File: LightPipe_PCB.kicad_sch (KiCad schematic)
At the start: 13 parts, among them J5 AudioJack4, X1 KLB-4, X2 KLB-4, X3 XT30, X4.1 Cable-0.7mm, X4.2 Cable-0.7mm, X5.1 Cable-1.5mm, X5.2 Cable-1.5mm

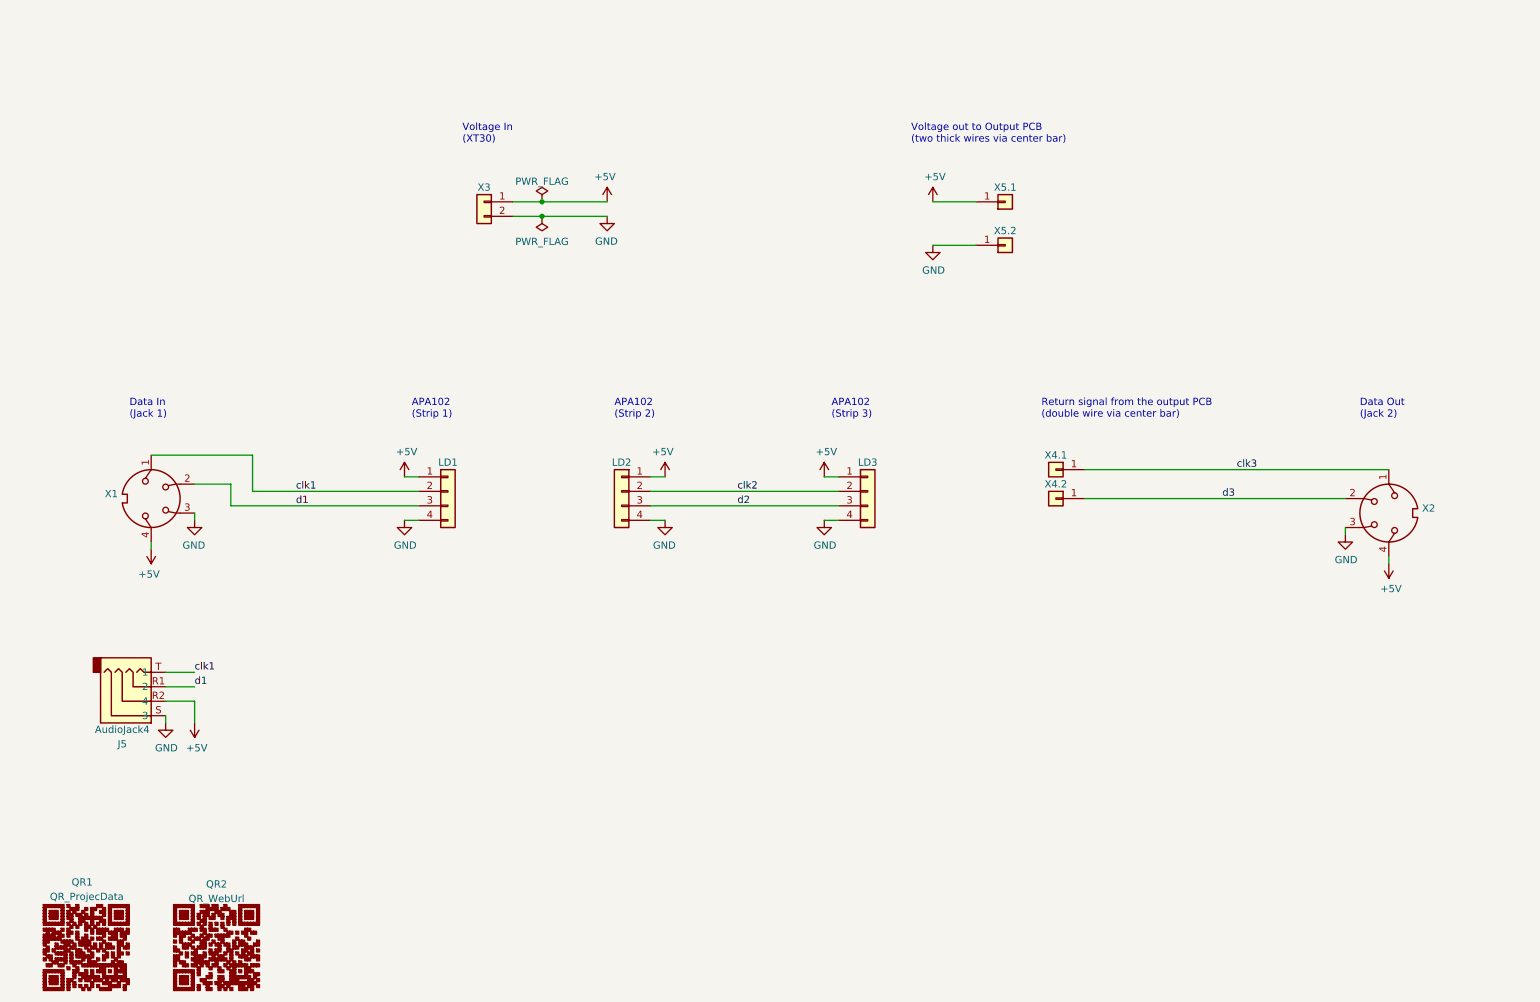
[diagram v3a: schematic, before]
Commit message: [clean] improved schematic and pcb to be easier to read in Input-Mode 2
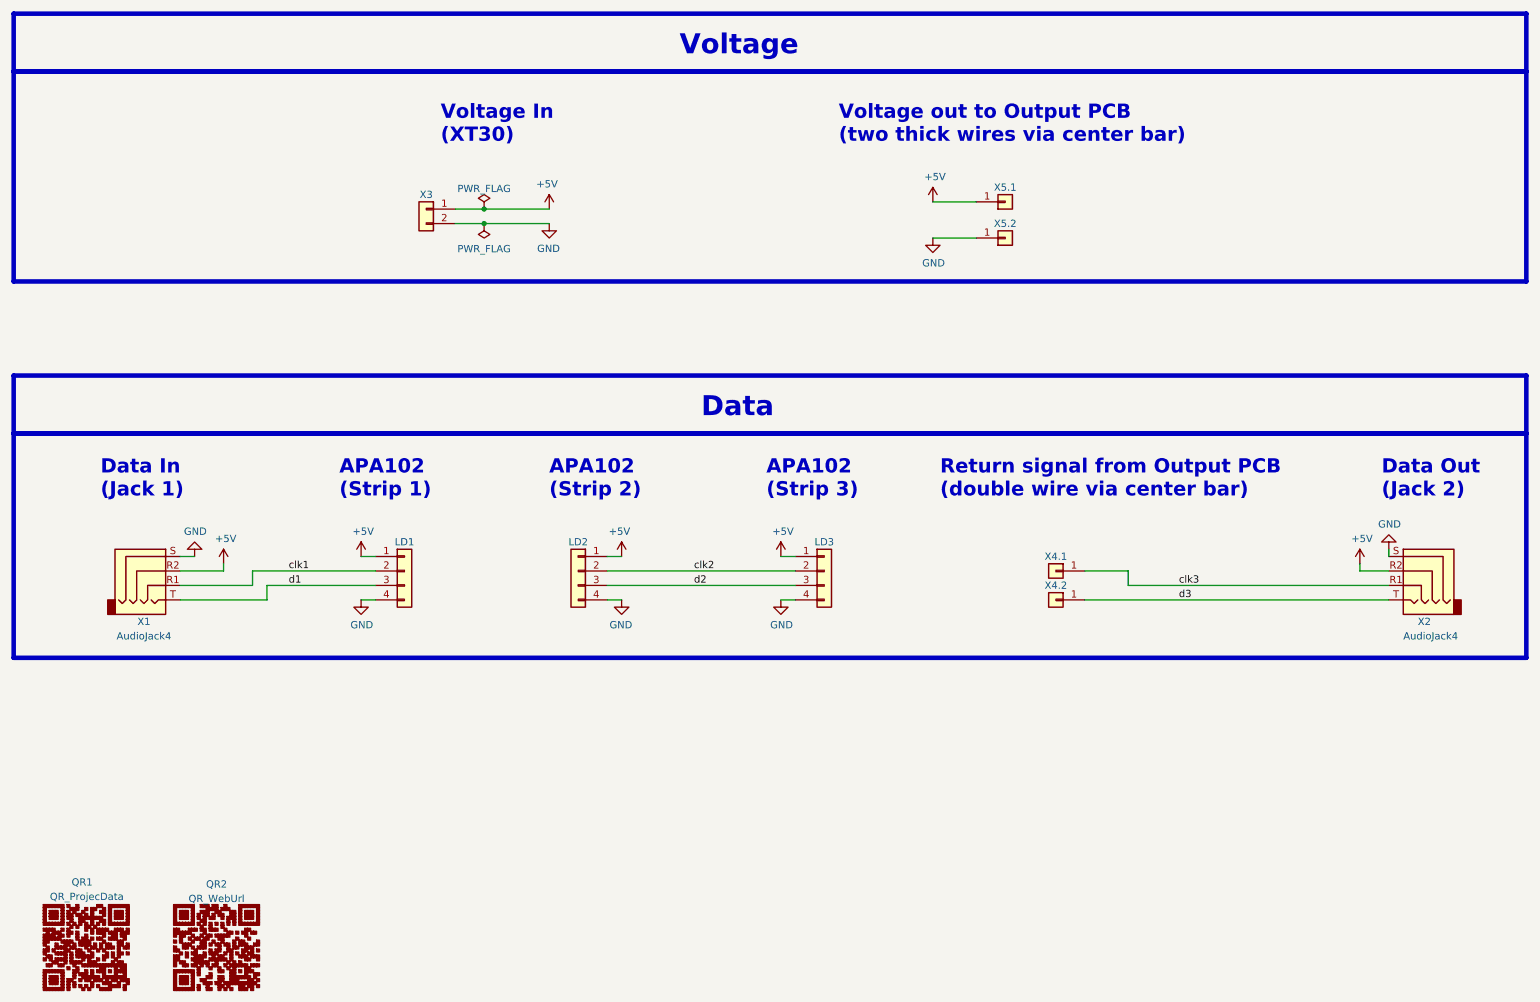
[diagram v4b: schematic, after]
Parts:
- removed X1, X2: KLB-4, h8-Connectors:Lumberg-KLB-4-Klinkensteckverbinder-3_5-180deg-turnable, symbol Connector:DIN-4
- added X2: AudioJack4, h8-Connectors:Lumberg-KLB-4-Jack-3_5-180deg-turnable, symbol Connector:AudioJack4
- QR1: footprint QR:QR_ProjecData -> QR_Lib:QR_ProjecData
- QR2: footprint QR:QR_WebUrl -> QR_Lib:QR_WebUrl
- X1: renamed from J5; footprint h8-Connectors:Lumberg-KLB-4-Klinkensteckverbinder-3_5-180deg-turnable -> h8-Connectors:Lumberg-KLB-4-Jack-3_5-180deg-turnable
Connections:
- net +5V: now also X2.R2
- net GND: now also X2.S
- net clk1: now also X1.R1; no longer X1.T
- net clk3: now also X2.R1
- net d1: now also X1.T; no longer X1.R1
- net d3: now also X2.T
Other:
- note added: "Data"
- note added: "Return signal from Output PCB (double wire via center bar)"
- note added: "Voltage"
- note removed: "Return signal from the output PCB (double wire via center bar)"
- moved on the sheet: LD1, LD2, LD3, X3, X4.1, X4.2, X5.2

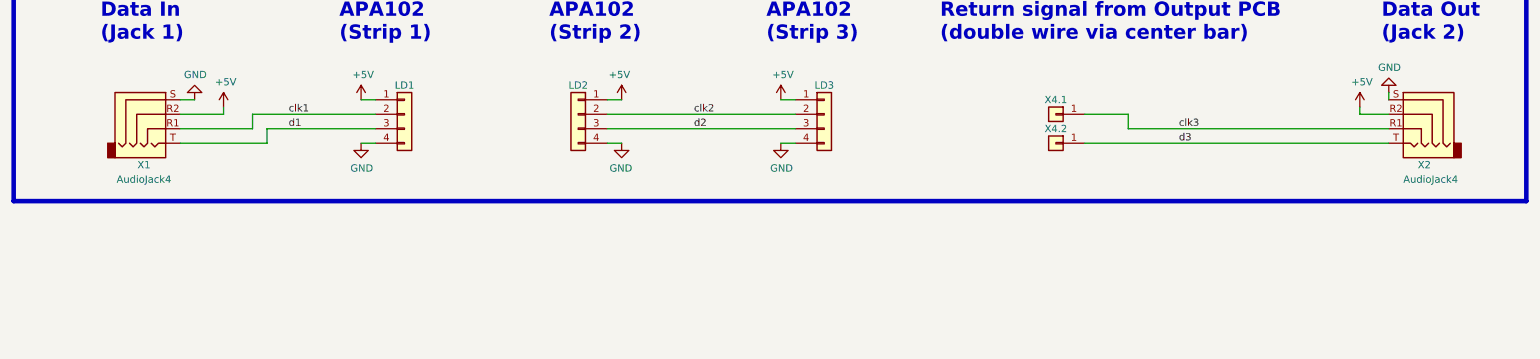
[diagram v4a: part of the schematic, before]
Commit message: [PCB] Fixed Fab layers | added attributes to components
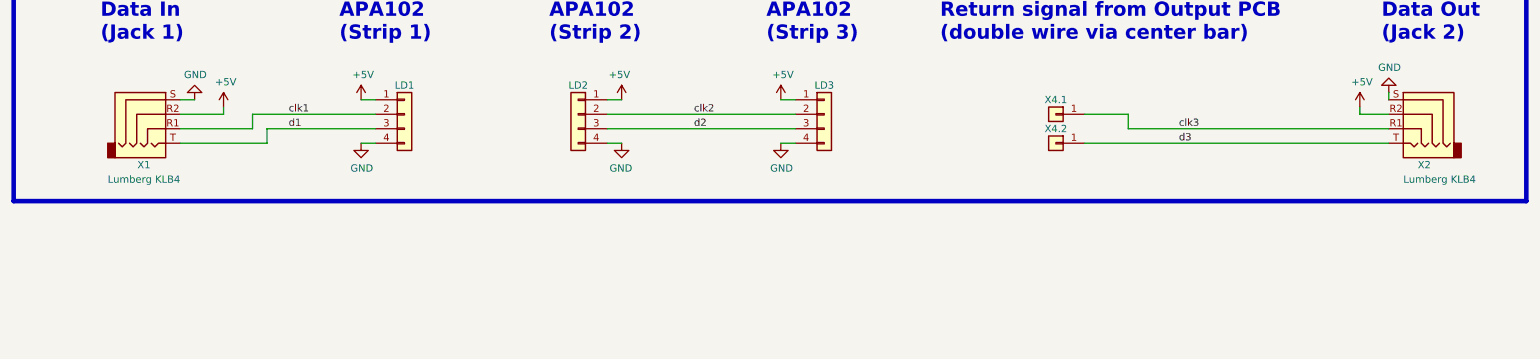
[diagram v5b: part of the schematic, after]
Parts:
- X1, X2: value AudioJack4 -> Lumberg KLB4; MF (none) -> Lumberg; MF1 (none) -> HUXUAN; MFN (none) -> KLB4; MFN1 (none) -> PJ392
- X3: LCSC (none) -> C108769; MF (none) -> Changzhou Amass Elec; MFN (none) -> XT30UPB30-F.G.*
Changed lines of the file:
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@@
       (effects (font (size 1.27 1.27)) hide)
     )
-    (property "Datasheet" "~" (id 3) (at 87.63 54.61 0)
+    (property "Datasheet" "https://datasheet.lcsc.com/lcsc/2207151430_Changzhou-Amass-Elec-XT30UPB30-F-G--_C108769.pdf" (id 3) (at 87.63 54.61 0)
+      (effects (font (size 1.27 1.27)) hide)
+    )
+    (property "MF" "Changzhou Amass Elec " (id 4) (at 87.63 54.61 0)
+      (effects (font (size 1.27 1.27)) hide)
+    )
+    (property "MFN" "XT30UPB30-F.G.*" (id 5) (at 87.63 54.61 0)
+      (effects (font (size 1.27 1.27)) hide)
+    )
+    (property "LCSC" "C108769" (id 6) (at 87.63 54.61 0)
       (effects (font (size 1.27 1.27)) hide)
     )
@@
     (in_bom yes) (on_board yes)
     (property "Reference" "X1" (id 0) (at 38.1 127 0))
-    (property "Value" "AudioJack4" (id 1) (at 38.1 129.54 0))
+    (property "Value" "Lumberg KLB4" (id 1) (at 38.1 129.54 0))
     (property "Footprint" "h8-Connectors:Lumberg-KLB-4-Jack-3_5-180deg-turnable" (id 2) (at 39.37 118.11 0)
       (effects (font (size 1.27 1.27)) hide)
     )
-    (property "Datasheet" "~" (id 3) (at 39.37 118.11 0)
+    (property "Datasheet" "https://downloads.lumberg.com/datenblaetter/en/klb4.pdf" (id 3) (at 39.37 118.11 0)
+      (effects (font (size 1.27 1.27)) hide)
+    )
+    (property "MF" "Lumberg" (id 4) (at 39.37 118.11 0)
+      (effects (font (size 1.27 1.27)) hide)
+    )
+    (property "MFN" "KLB4" (id 5) (at 39.37 118.11 0)
+      (effects (font (size 1.27 1.27)) hide)
+    )
+    (property "MF1" "HUXUAN" (id 6) (at 39.37 118.11 0)
+      (effects (font (size 1.27 1.27)) hide)
+    )
+    (property "MFN1" "PJ392" (id 7) (at 39.37 118.11 0)
       (effects (font (size 1.27 1.27)) hide)
     )
@@
       (effects (font (size 1.27 1.27)) (justify right))
     )
-    (property "Value" "AudioJack4" (id 1) (at 259.08 129.54 0)
+    (property "Value" "Lumberg KLB4" (id 1) (at 259.08 129.54 0)
       (effects (font (size 1.27 1.27)) (justify right))
     )
@@
       (effects (font (size 1.27 1.27)) hide)
     )
-    (property "Datasheet" "~" (id 3) (at 261.62 118.11 0)
+    (property "Datasheet" "https://downloads.lumberg.com/datenblaetter/en/klb4.pdf" (id 3) (at 261.62 118.11 0)
+      (effects (font (size 1.27 1.27)) hide)
+    )
+    (property "MF" "Lumberg" (id 4) (at 261.62 118.11 0)
+      (effects (font (size 1.27 1.27)) hide)
+    )
+    (property "MFN" "KLB4" (id 5) (at 261.62 118.11 0)
+      (effects (font (size 1.27 1.27)) hide)
+    )
+    (property "MF1" "HUXUAN" (id 6) (at 261.62 118.11 0)
+      (effects (font (size 1.27 1.27)) hide)
+    )
+    (property "MFN1" "PJ392" (id 7) (at 261.62 118.11 0)
       (effects (font (size 1.27 1.27)) hide)
     )
@@
     )
     (path "/67e54464-02b8-42b4-98cc-9748abe49e4c"
-      (reference "X1") (unit 1) (value "AudioJack4") (footprint "h8-Connectors:Lumberg-KLB-4-Jack-3_5-180deg-turnable")
+      (reference "X1") (unit 1) (value "Lumberg KLB4") (footprint "h8-Connectors:Lumberg-KLB-4-Jack-3_5-180deg-turnable")
     )
     (path "/7f404442-9c89-47ea-a816-5ae74e1d23ad"
-      (reference "X2") (unit 1) (value "AudioJack4") (footprint "h8-Connectors:Lumberg-KLB-4-Jack-3_5-180deg-turnable")
+      (reference "X2") (unit 1) (value "Lumberg KLB4") (footprint "h8-Connectors:Lumberg-KLB-4-Jack-3_5-180deg-turnable")
     )
     (path "/00000000-0000-0000-0000-00005f94666b"

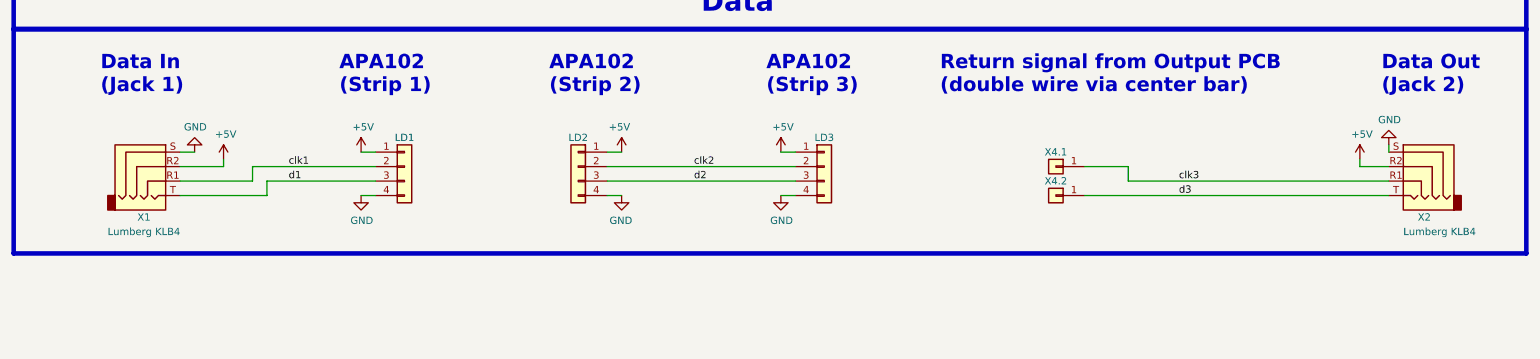
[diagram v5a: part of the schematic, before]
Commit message: [WIP] Optimize PCB for more common LED-Strip (GND, D, CLK, 5V)
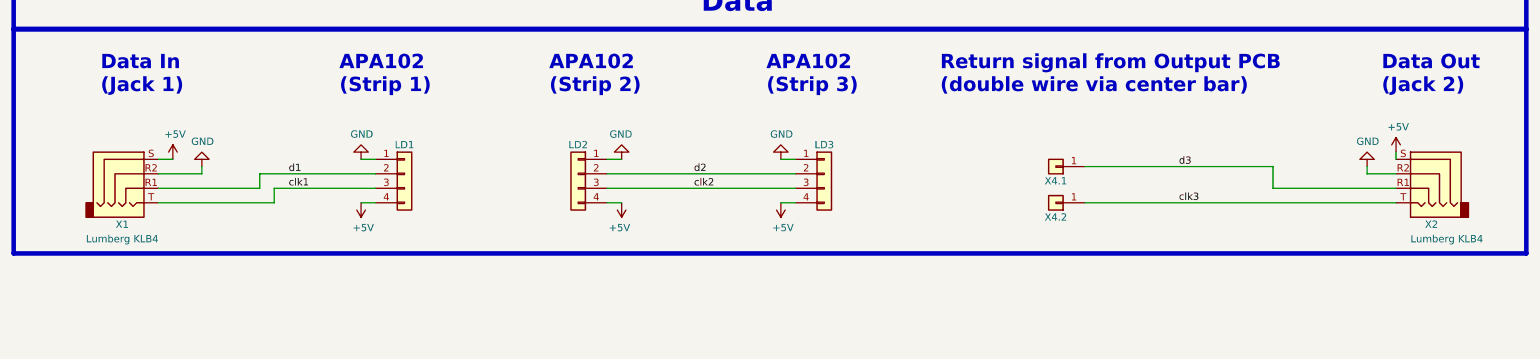
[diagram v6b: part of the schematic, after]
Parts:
- renumbered X5.2 to X5.1, X5.1 to X5.2
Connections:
- net +5V: now also LD1.4 (Pin_4), LD2.4 (Pin_4), LD3.4 (Pin_4), X1.S, X2.S, X5.1.1 (Pin_1); no longer LD1.1 (Pin_1), LD2.1 (Pin_1), LD3.1 (Pin_1), X1.R2, X2.R2, X5.2.1 (Pin_1)
- net GND: now also LD1.1 (Pin_1), LD2.1 (Pin_1), LD3.1 (Pin_1), X1.R2, X2.R2, X5.2.1 (Pin_1); no longer LD1.4 (Pin_4), LD2.4 (Pin_4), LD3.4 (Pin_4), X1.S, X2.S, X5.1.1 (Pin_1)
- net clk1: now also LD1.3 (Pin_3), X1.T; no longer LD1.2 (Pin_2), X1.R1
- net clk2: now also LD2.3 (Pin_3), LD3.3 (Pin_3); no longer LD2.2 (Pin_2), LD3.2 (Pin_2)
- net clk3: now also X2.T, X4.2.1 (Pin_1); no longer X2.R1, X4.1.1 (Pin_1)
- net d1: now also LD1.2 (Pin_2), X1.R1; no longer LD1.3 (Pin_3), X1.T
- net d2: now also LD2.2 (Pin_2), LD3.2 (Pin_2); no longer LD2.3 (Pin_3), LD3.3 (Pin_3)
- net d3: now also X2.R1, X4.1.1 (Pin_1); no longer X2.T, X4.2.1 (Pin_1)
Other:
- moved on the sheet: LD1, LD2, LD3, X1, X2, X4.1, X4.2, X5.1, X5.2
